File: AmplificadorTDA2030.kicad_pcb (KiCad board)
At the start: 2 copper layers, 70 x 70 mm, 36 parts, among them J1 SJ1-3523N, J2 DC-005, J3 Speaker, U1 TDA2030, U2 TDA2030

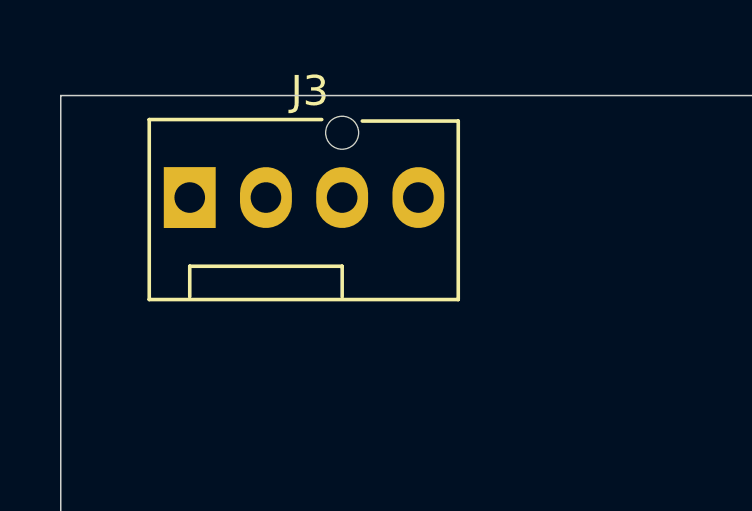
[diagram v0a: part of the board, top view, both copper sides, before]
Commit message: Se agrega Esquematico y BOM
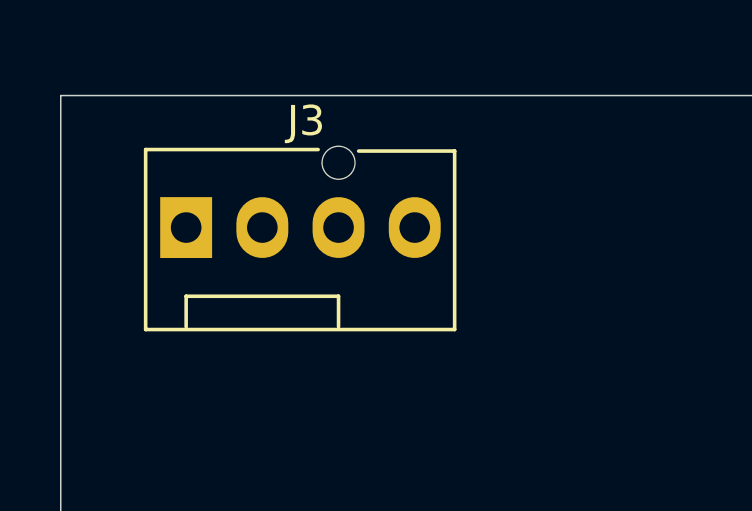
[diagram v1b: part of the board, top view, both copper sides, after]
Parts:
- moved J3 1.01 mm to (116.2, 62.2)
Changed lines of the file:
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@@
 	(footprint "Connector:FanPinHeader_1x04_P2.54mm_Vertical"
 		(layer "F.Cu")
-		(at 116.3 61.2)
+		(at 116.18 62.2)
 		(descr "4-pin CPU fan Through hole pin header, e.g. for Wieson part number 2366C888-007 Molex 47053-1000, Foxconn HF27040-M1, Tyco 1470947-1 or equivalent, see http://www.formfactors.org/developer%5Cspecs%5Crev1_2_public.pdf")
 		(tags "pin header 4-pin CPU fan")
@@
 		(at 170.06 115.95 90)
 		(property "Reference" "J2"
-			(at -8.26 -5.71721 270)
+			(at -8.26 -5.71721 -90)
 			(layer "F.SilkS")
 			(effects
@@
 		)
 		(property "Value" "DC-005"
-			(at -3.1848 7.6271 270)
-			(layer "F.Fab")
-			(effects
+			(at -3.1848 7.6271 -90)
+			(layer "F.Fab")
+			(effects

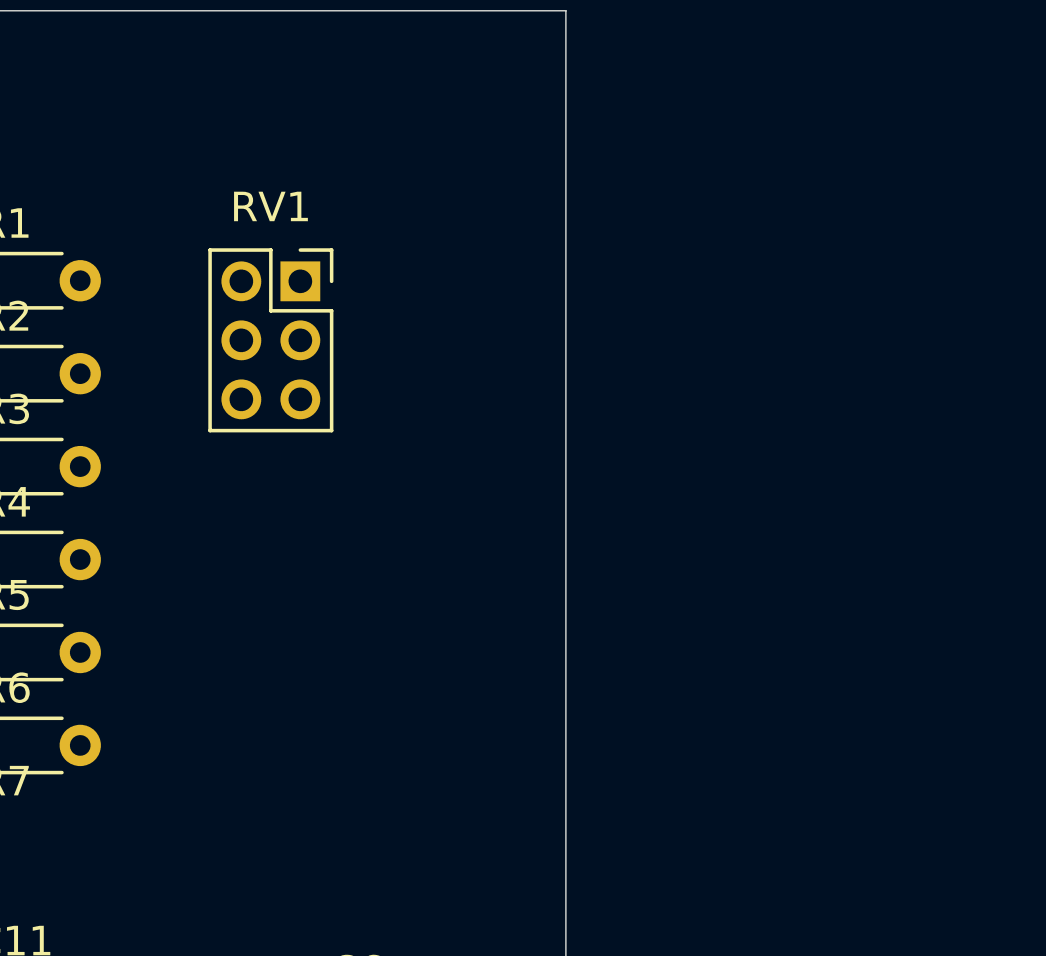
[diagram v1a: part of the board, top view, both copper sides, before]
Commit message: Librerias de Simbolos,Footprints y Modelos 3D Agregados
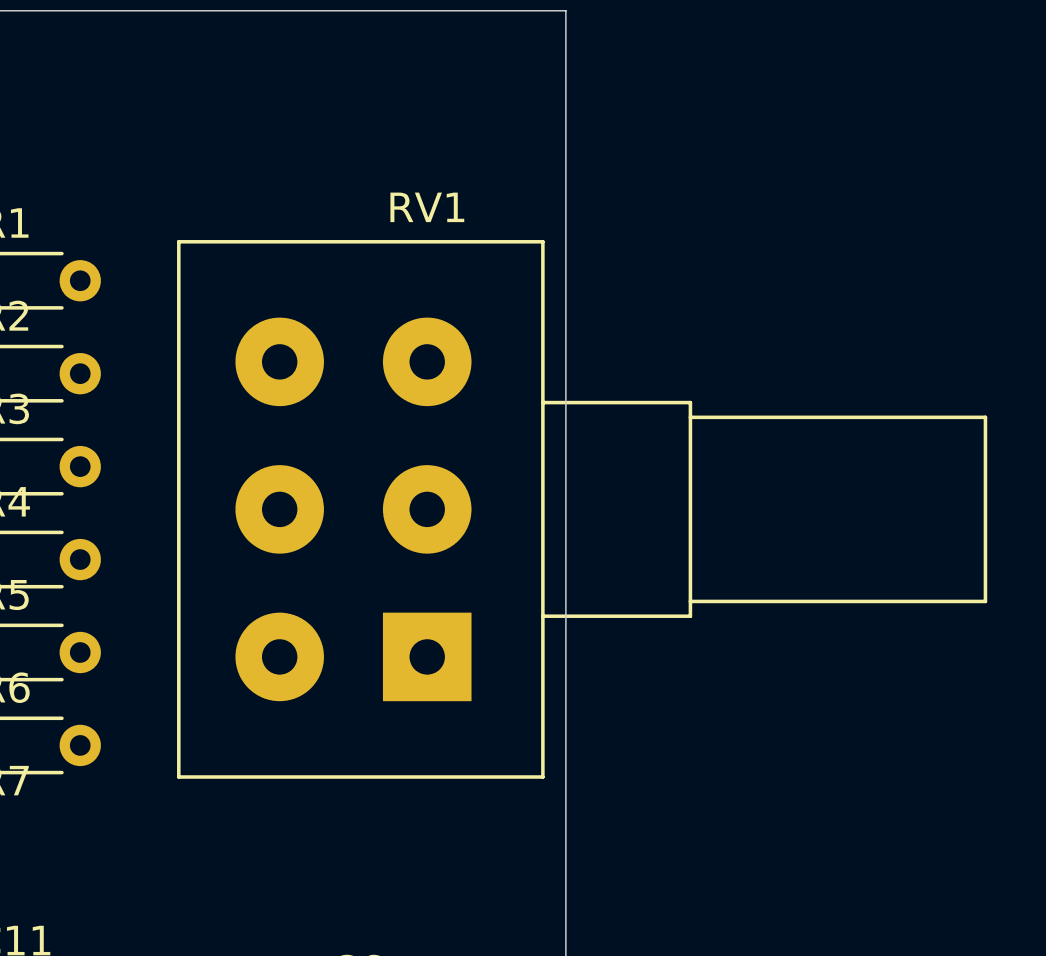
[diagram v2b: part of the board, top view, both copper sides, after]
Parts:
- J2: footprint Footprints y Simbolos:NINIGI_DC-005 -> DC-005 - Connector Alimentacion:NINIGI_DC-005
- RV1: footprint Connector_PinSocket_2.00mm:PinSocket_2x03_P2.00mm_Vertical -> Potentiometer_THT:Potentiometer_Alps_RK163_Dual_Horizontal
- moved RV1 13.4 mm to (177.3, 79.7), turned to 180 degrees
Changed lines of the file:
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@@
 		)
 	)
-	(footprint "Footprints y Simbolos:NINIGI_DC-005"
+	(footprint "DC-005 - Connector Alimentacion:NINIGI_DC-005"
 		(layer "F.Cu")
 		(at 170.06 115.95 90)
 		(property "Reference" "J2"
-			(at -8.26 -5.71721 -90)
+			(at -8.26 -5.71721 90)
 			(layer "F.SilkS")
 			(effects
@@
 		)
 		(property "Value" "DC-005"
-			(at -3.1848 7.6271 -90)
+			(at -3.1848 7.6271 90)
 			(layer "F.Fab")
 			(effects
@@
 			)
 		)
-		(property "Footprint" "Footprints y Simbolos:NINIGI_DC-005"
+		(property "Footprint" "DC-005 - Connector Alimentacion:NINIGI_DC-005"
 			(at 0 0 90)
 			(unlocked yes)
@@
 			(solder_mask_margin 0.102)
 		)
-		(model "${KICAD8_3DMODEL_DIR}/Modelos3D_Emanuel/DC-005.step"
+		(model "${KIPRJMOD}/Lib/3DModels/DC-005 Conector/DC-005.step"
 			(offset
 				(xyz -4 0 0)
@@
 		)
 	)
-	(footprint "Connector_PinSocket_2.00mm:PinSocket_2x03_P2.00mm_Vertical"
+	(footprint "Potentiometer_THT:Potentiometer_Alps_RK163_Dual_Horizontal"
 		(layer "F.Cu")
-		(at 173 66.97)
-		(descr "Through hole straight socket strip, 2x03, 2.00mm pitch, double cols (from Kicad 4.0.7), script generated")
-		(tags "Through hole socket strip THT 2x03 2.00mm double row")
+		(at 177.3 79.7 180)
+		(descr "12101A2 1210AX9 12A0B85 12A0BKR  Potentiometer, horizontal, Alps RK163 Dual, https://tech.alpsalpine.com/prod/e/pdf/potentiometer/rotarypotentiometers/rk16/rk16.pdf")
+		(tags "Potentiometer horizontal Alps RK163 Dual")
 		(property "Reference" "RV1"
-			(at -1 -2.5 0)
+			(at -0.000001 15.199999 180)
 			(layer "F.SilkS")
 			(effects
@@
 		)
 		(property "Value" "A50K"
-			(at -1 6.5 0)
+			(at 0 -5.2 180)
 			(layer "F.Fab")
 			(effects
@@
 			)
 		)
-		(property "Footprint" "Connector_PinSocket_2.00mm:PinSocket_2x03_P2.00mm_Vertical"
-			(at 0 0 0)
+		(property "Footprint" "Potentiometer_THT:Potentiometer_Alps_RK163_Dual_Horizontal"
+			(at 0 0 180)
 			(unlocked yes)
 			(layer "F.Fab")
@@
 		)
 		(property "Datasheet" ""
-			(at 0 0 0)
+			(at 0 0 180)
 			(unlocked yes)
 			(layer "F.Fab")
@@
 		)
 		(property "Description" "Dual potentiometer"
-			(at 0 0 0)
+			(at 0 0 180)
 			(unlocked yes)
 			(layer "F.Fab")
@@
 		(attr through_hole)
 		(fp_line
-			(start -3.06 -1.06)
-			(end -3.06 5.06)
+			(start 8.42 14.07)
+			(end 8.42 -4.07)
+			(stroke
+				(width 0.12)
+				(type solid)
+			)
+			(layer "F.SilkS")
+		)
+		(fp_line
+			(start 8.42 14.07)
+			(end -3.92 14.07)
 			(stroke
 				(width 0.12)
@@
 		)
 		(fp_line
-			(start -3.06 -1.06)
-			(end -1 -1.06)
+			(start 8.42 -4.07)
+			(end -3.92 -4.07)
 			(stroke
 				(width 0.12)
@@
 		)
 		(fp_line
-			(start -3.06 5.06)
-			(end 1.06 5.06)
+			(start -3.92 14.07)
+			(end -3.92 -4.07)
 			(stroke
 				(width 0.12)
@@
 		)
 		(fp_line
-			(start -1 -1.06)
-			(end -1 1)
+			(start -3.92 8.62)
+			(end -8.92 8.62)
 			(stroke
 				(width 0.12)
@@
 		)
 		(fp_line
-			(start -1 1)
-			(end 1.06 1)
+			(start -3.92 1.38)
+			(end -8.92 1.38)
 			(stroke
 				(width 0.12)
@@
 		)
 		(fp_line
-			(start 0 -1.06)
-			(end 1.06 -1.06)
+			(start -8.92 8.62)
+			(end -8.92 1.38)
 			(stroke
 				(width 0.12)
@@
 		)
 		(fp_line
-			(start 1.06 -1.06)
-			(end 1.06 0)
+			(start -8.92 8.12)
+			(end -18.92 8.12)
 			(stroke
 				(width 0.12)
@@
 		)
 		(fp_line
-			(start 1.06 1)
-			(end 1.06 5.06)
+			(start -8.92 1.88)
+			(end -18.92 1.88)
 			(stroke
 				(width 0.12)
@@
 		)
 		(fp_line
-			(start -3.5 -1.5)
-			(end 1.5 -1.5)
+			(start -18.92 8.12)
+			(end -18.92 1.88)
+			(stroke
+				(width 0.12)
+				(type solid)
+			)
+			(layer "F.SilkS")
+		)
+		(fp_line
+			(start 8.55 14.2)
+			(end 8.55 -4.2)
 			(stroke
 				(width 0.05)
@@
 		)
 		(fp_line
-			(start -3.5 5.5)
-			(end -3.5 -1.5)
+			(start 8.55 -4.2)
+			(end -19.05 -4.2)
 			(stroke
 				(width 0.05)
@@
 		)
 		(fp_line
-			(start 1.5 -1.5)
-			(end 1.5 5.5)
+			(start -19.05 14.2)
+			(end 8.55 14.2)
 			(stroke
 				(width 0.05)
@@
 		)
 		(fp_line
-			(start 1.5 5.5)
-			(end -3.5 5.5)
+			(start -19.05 -4.2)
+			(end -19.05 14.2)
 			(stroke
 				(width 0.05)
@@
 		)
 		(fp_line
-			(start -3 -1)
-			(end 0 -1)
+			(start 8.3 13.95)
+			(end 8.3 -3.95)
+			(stroke
+				(width 0.1)
+				(type solid)
+			)
+			(layer "F.Fab")
+		)
+		(fp_line
+			(start 8.3 -3.95)
+			(end -3.8 -3.95)
+			(stroke
+				(width 0.1)
+				(type solid)
+			)
+			(layer "F.Fab")
+		)
+		(fp_line
+			(start -3.8 13.95)
+			(end 8.3 13.95)
+			(stroke
+				(width 0.1)
+				(type solid)
+			)
+			(layer "F.Fab")
+		)
+		(fp_line
+			(start -3.8 1.5)
+			(end -8.8 1.5)
+			(stroke
+				(width 0.1)
+				(type solid)
+			)
+			(layer "F.Fab")
+		)
+		(fp_line
+			(start -3.8 -3.95)
+			(end -3.8 13.95)
 			(stroke
 				(width 0.1)
@@
 		)
 		(fp_line
-			(start -3 5)
-			(end -3 -1)
+			(start -8.8 8.5)
+			(end -3.8 8.5)
 			(stroke
 				(width 0.1)
@@
 		)
 		(fp_line
-			(start 0 -1)
-			(end 1 0)
+			(start -8.8 2)
+			(end -18.8 2)
 			(stroke
 				(width 0.1)
@@
 		)
 		(fp_line
-			(start 1 0)
-			(end 1 5)
+			(start -8.8 1.5)
+			(end -8.8 8.5)
 			(stroke
 				(width 0.1)
@@
 		)
 		(fp_line
-			(start 1 5)
-			(end -3 5)
+			(start -18.8 8)
+			(end -8.8 8)
+			(stroke
+				(width 0.1)
+				(type solid)
+			)
+			(layer "F.Fab")
+		)
+		(fp_line
+			(start -18.8 2)
+			(end -18.8 8)
 			(stroke
 				(width 0.1)
@@
 		)
 		(fp_text user "${REFERENCE}"
-			(at -1 2 90)
+			(at 2.25 5 180)
 			(layer "F.Fab")
 			(effects
@@
 		(pad "1" thru_hole rect
 			(at 0 0)
-			(size 1.35 1.35)
-			(drill 0.8)
+			(size 3 3)
+			(drill 1.2)
 			(layers "*.Cu" "*.Mask")
 			(remove_unused_layers no)
@@
 			(pintype "passive")
 		)
-		(pad "2" thru_hole oval
-			(at -2 0)
-			(size 1.35 1.35)
-			(drill 0.8)
+		(pad "2" thru_hole circle
+			(at 0 5)
+			(size 3 3)
+			(drill 1.2)
 			(layers "*.Cu" "*.Mask")
 			(remove_unused_layers no)
@@
 			(pintype "passive")
 		)
-		(pad "3" thru_hole oval
-			(at 0 2)
-			(size 1.35 1.35)
-			(drill 0.8)
+		(pad "3" thru_hole circle
+			(at 0 10)
+			(size 3 3)
+			(drill 1.2)
 			(layers "*.Cu" "*.Mask")
 			(remove_unused_layers no)
@@
 			(pintype "passive")
 		)
-		(pad "4" thru_hole oval
-			(at -2 2)
-			(size 1.35 1.35)
-			(drill 0.8)
+		(pad "4" thru_hole circle
+			(at 5 0)
+			(size 3 3)
+			(drill 1.2)
 			(layers "*.Cu" "*.Mask")
 			(remove_unused_layers no)
@@
 			(pintype "passive")
 		)
-		(pad "5" thru_hole oval
-			(at 0 4)
-			(size 1.35 1.35)
-			(drill 0.8)
+		(pad "5" thru_hole circle
+			(at 5 5)
+			(size 3 3)
+			(drill 1.2)
 			(layers "*.Cu" "*.Mask")
 			(remove_unused_layers no)
@@
 			(pintype "passive")
 		)
-		(pad "6" thru_hole oval
-			(at -2 4)
-			(size 1.35 1.35)
-			(drill 0.8)
+		(pad "6" thru_hole circle
+			(at 5 10)
+			(size 3 3)
+			(drill 1.2)
 			(layers "*.Cu" "*.Mask")
 			(remove_unused_layers no)
@@
 			(pintype "passive")
 		)
-		(model "${KICAD8_3DMODEL_DIR}/Connector_PinSocket_2.00mm.3dshapes/PinSocket_2x03_P2.00mm_Vertical.wrl"
+		(model "${KICAD8_3DMODEL_DIR}/Potentiometer_THT.3dshapes/Potentiometer_Alps_RK163_Dual_Horizontal.wrl"
 			(offset
 				(xyz 0 0 0)
@@
 			)
 		)
+		(model "${KIPRJMOD}/Lib/3DModels/Potencimetros/potenciometro_doble.STEP"
+			(offset
+				(xyz 6 -5 11.5)
+			)
+			(scale
+				(xyz 1 1 0.8)
+			)
+			(rotate
+				(xyz -90 0 90)
+			)
+		)
 	)
 	(footprint "Package_TO_SOT_THT:TO-220-5_P3.4x3.7mm_StaggerOdd_Lead3.8mm_Vertical"
@@
 			(solder_mask_margin 0.102)
 		)
-		(model "G:/Mi unidad/Proyectos/Modelos 3D/CUI_DEVICES_SJ1-3523N/CUI_DEVICES_SJ1-3523N.step"
+		(model "${KIPRJMOD}/Lib/3DModels/CUI_DEVICES_SJ1-3523N/CUI_DEVICES_SJ1-3523N.step"
 			(offset
 				(xyz 0 -6.8 3)

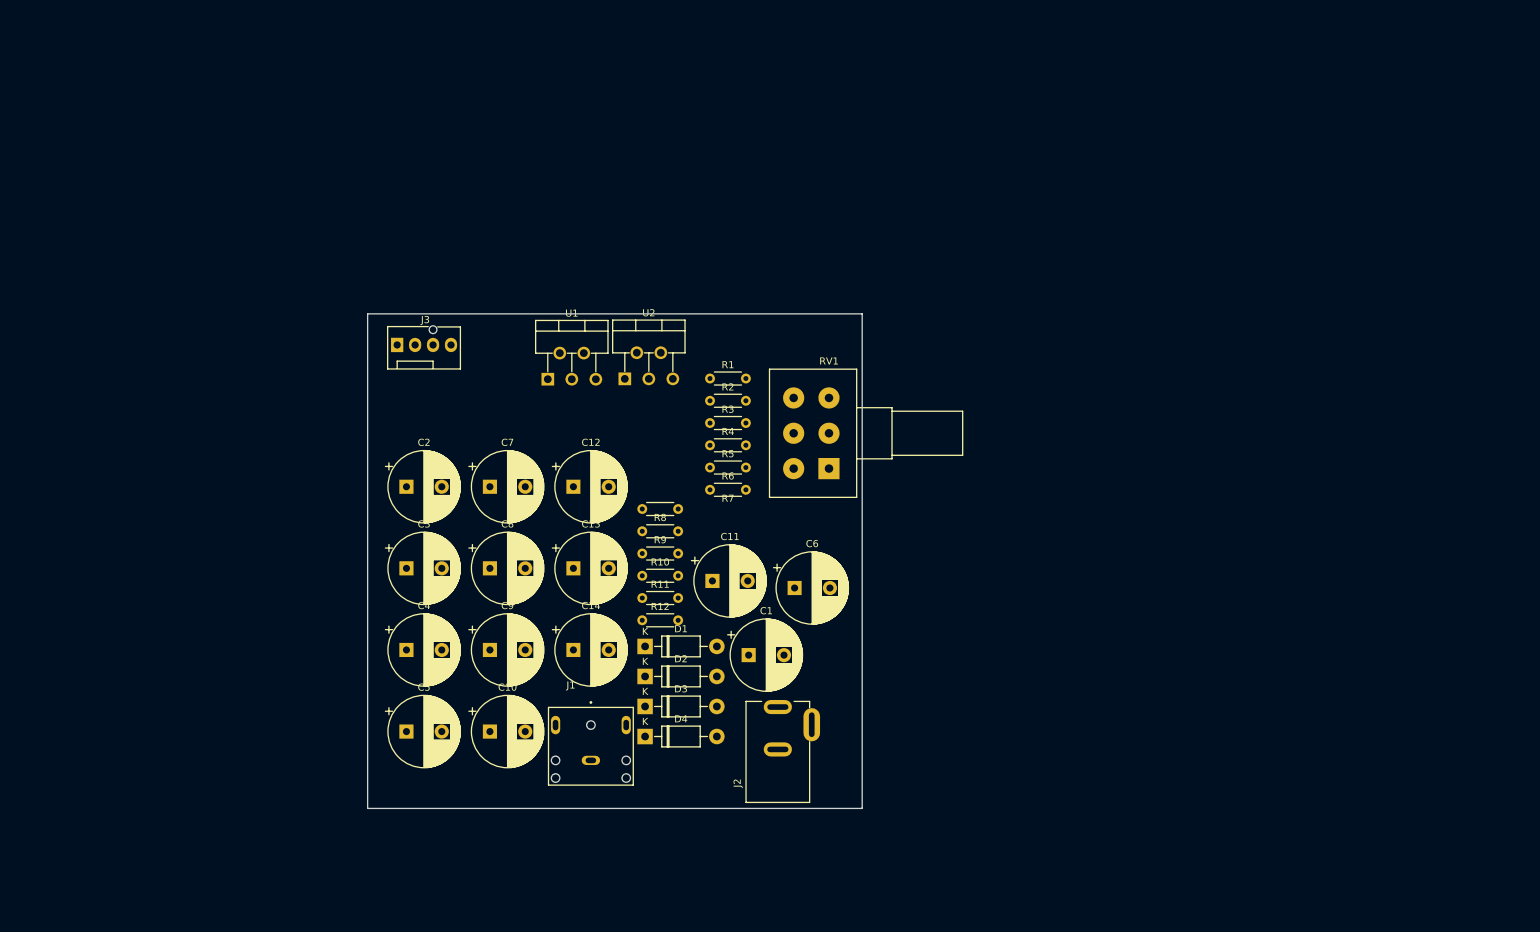
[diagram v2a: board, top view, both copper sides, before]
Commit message: Footprints Asignados
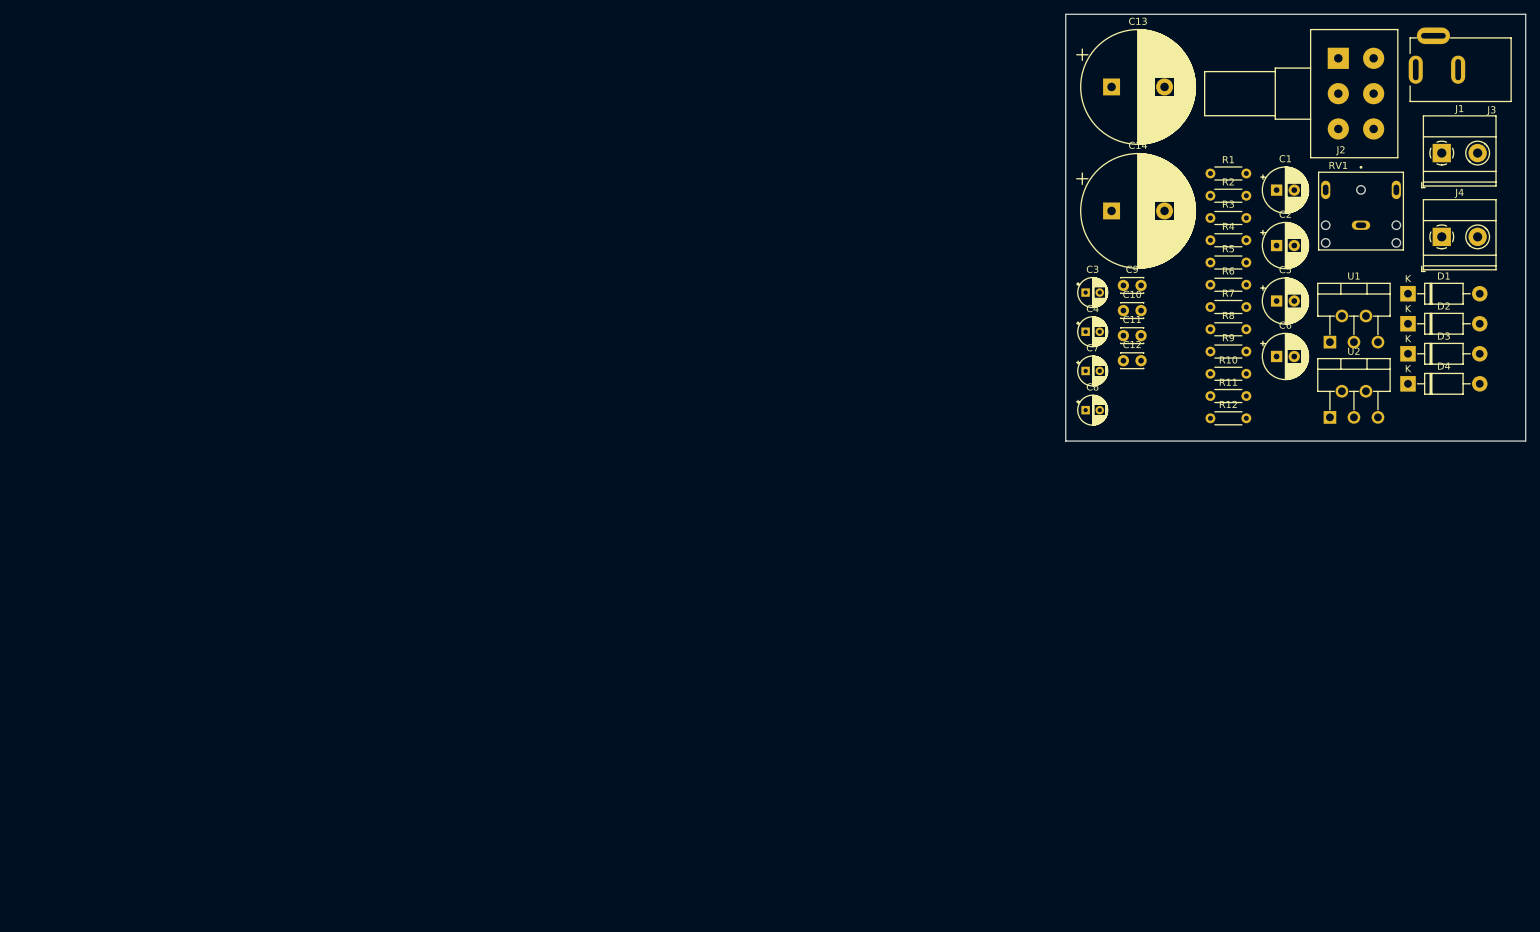
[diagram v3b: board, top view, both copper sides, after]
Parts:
- added J4: L_Speaker, TerminalBlock_Phoenix:TerminalBlock_Phoenix_MKDS-1,5-2-5.08_1x02_P5.08mm_Horizontal, F.Cu at (264.0, 46.9)
- C1, C2, C5, C6: footprint Capacitor_THT:CP_Radial_D10.0mm_P5.00mm -> Capacitor_THT:CP_Radial_D6.3mm_P2.50mm
- C10, C11, C12, C9: footprint Capacitor_THT:CP_Radial_D10.0mm_P5.00mm -> Capacitor_THT:C_Disc_D3.0mm_W2.0mm_P2.50mm
- C13, C14: value 2000uF -> 2200uF; footprint Capacitor_THT:CP_Radial_D10.0mm_P5.00mm -> Capacitor_THT:CP_Radial_D16.0mm_P7.50mm
- C3, C4, C7, C8: footprint Capacitor_THT:CP_Radial_D10.0mm_P5.00mm -> Capacitor_THT:CP_Radial_D4.0mm_P2.00mm
- J1: value SJ1-3523N -> R_Speaker; footprint SJ1-3523N:CUI_SJ1-3523N -> TerminalBlock_Phoenix:TerminalBlock_Phoenix_MKDS-1,5-2-5.08_1x02_P5.08mm_Horizontal
- J2: value DC-005 -> SJ1-3523N; footprint DC-005 - Connector Alimentacion:NINIGI_DC-005 -> SJ1-3523N:CUI_SJ1-3523N
- J3: value Speaker -> DC-005; footprint Connector:FanPinHeader_1x04_P2.54mm_Vertical -> DC-005 - Connector Alimentacion:NINIGI_DC-005
- moved J3 151.8 mm to (262.9, 23.2), turned to 180 degrees
- moved J1 148.0 mm to (264.0, 35.0)
- moved C5 137.4 mm to (240.7, 56.0)
- moved C2 127.8 mm to (240.7, 48.1)
- moved D1 119.0 mm to (259.2, 55.0)
- moved D2 119.0 mm to (259.2, 59.2)
- moved D3 119.0 mm to (259.2, 63.5)
- moved D4 119.0 mm to (259.2, 67.7)
- moved U1 110.8 mm to (248.2, 61.8)
- moved J2 108.7 mm to (252.6, 45.3), turned to 0 degrees
- moved C10 107.7 mm to (219.0, 57.3)
- moved C4 106.2 mm to (213.6, 60.3)
- moved C3 103.8 mm to (213.6, 54.8)
- moved C9 103.4 mm to (219.0, 53.8)
- moved C13 102.2 mm to (217.3, 25.7)
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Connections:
- J1 pad 2: Net-(J1-Pad2) -> /R_Output
- J2 pad 2: GND -> Net-(J2-Pad2)
- J2 pad 3: GND -> Net-(J2-Pad3)
- J3 pad 2: /L_Output -> GND
- J3 pad 4: GND -> /V+
- RV1 pad 1: Net-(J1-Pad2) -> Net-(J2-Pad2)
- RV1 pad 4: Net-(J1-Pad3) -> Net-(J2-Pad3)
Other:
- board size 70 x 70 mm -> 65.1 x 60.4 mm
